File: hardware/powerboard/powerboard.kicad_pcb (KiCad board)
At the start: 4 copper layers, 81.2 x 50.7 mm, 72 parts, among them J1 USB_B_Micro, J10 5V, J11 3V3, J2 Boot, J3 Keysboard Header, J4 Display, J5 Debug, J7 UART_0, J8 I2C_0, J9 I2C_1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

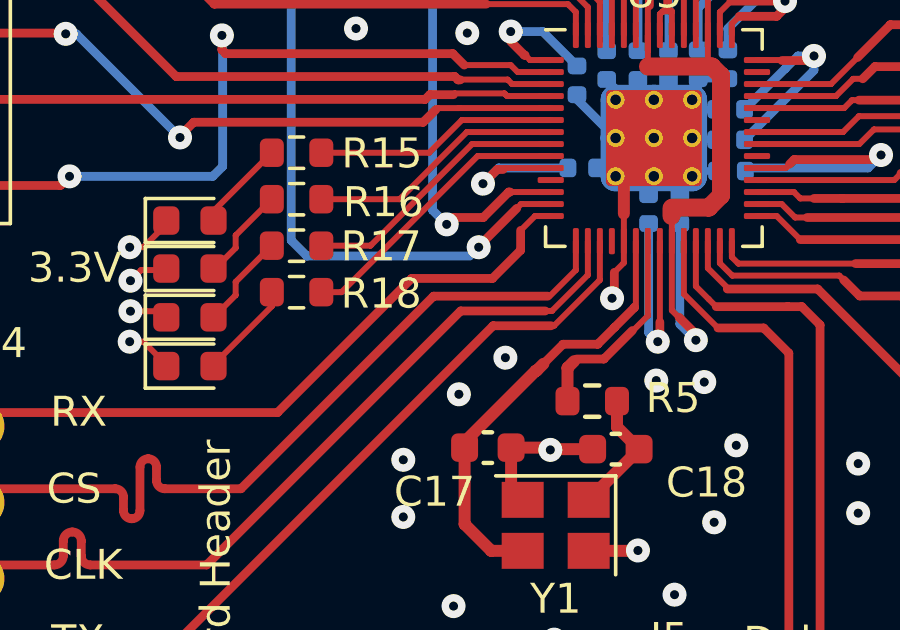
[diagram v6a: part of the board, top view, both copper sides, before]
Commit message: SPI_1 Pin error fixed
I'm a goof. The pins were off by 1. Rev. 1 will work with some additional wires. Rev. 2 will be ordered on my dime
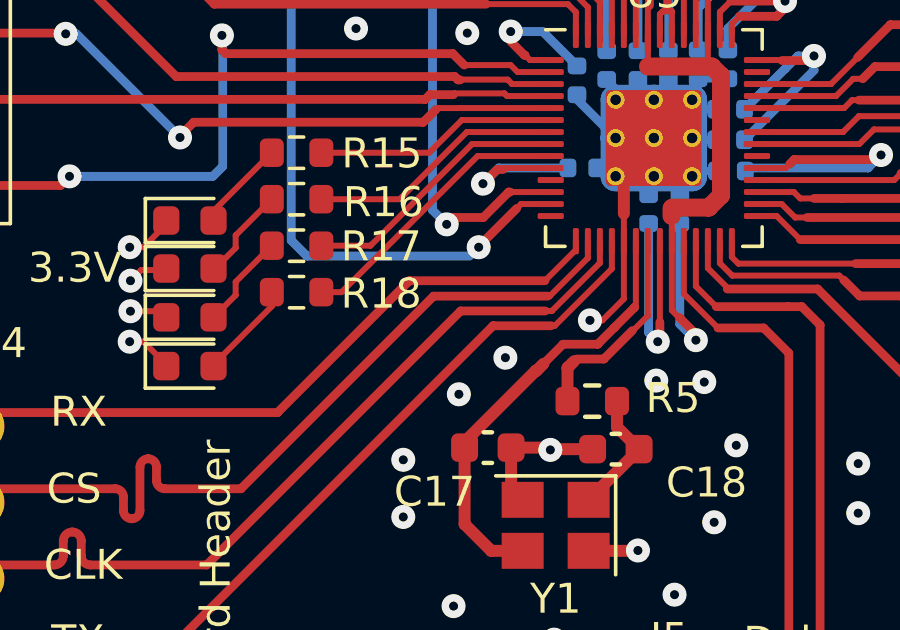
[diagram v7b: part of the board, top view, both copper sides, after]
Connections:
- U3 pad 14: SPI_RX_1 -> unconnected-(U3-Pad14)
- U3 pad 15: SPI_CS_1 -> SPI_RX_1
- U3 pad 16: SPI_SCLK_1 -> SPI_CS_1
- U3 pad 17: SPI_TX_1 -> SPI_SCLK_1
- U3 pad 18: unconnected-(U3-Pad18) -> SPI_TX_1
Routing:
- net GND: track 111.0 -> 112.3 mm

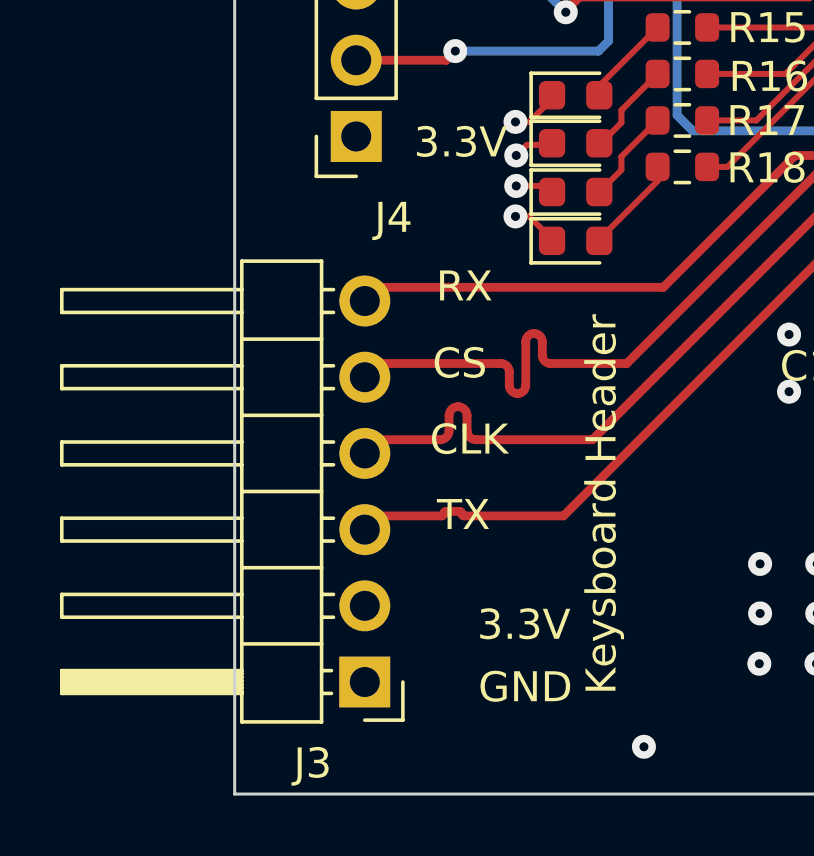
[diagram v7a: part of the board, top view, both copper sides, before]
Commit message: Rev.2 Boards Headers updated Male on Keysboard, Female on Brainboard
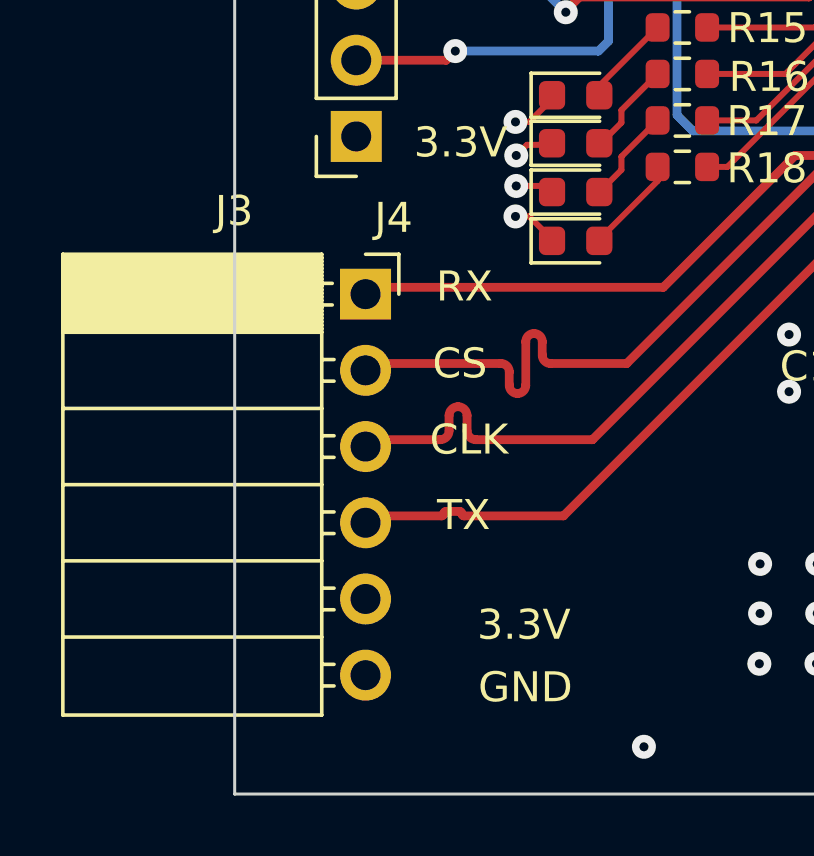
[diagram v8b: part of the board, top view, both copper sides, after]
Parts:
- J3: footprint Connector_PinHeader_2.54mm:PinHeader_1x06_P2.54mm_Horizontal -> Connector_PinSocket_2.54mm:PinSocket_1x06_P2.54mm_Horizontal
- moved J3 12.9 mm to (53.2, 49.2), turned to 0 degrees
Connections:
- J3 pad 1: GND -> SPI_RX_1
- J3 pad 2: +3.3V -> SPI_CS_1
- J3 pad 3: SPI_TX_1 -> SPI_SCLK_1
- J3 pad 4: SPI_SCLK_1 -> SPI_TX_1
- J3 pad 5: SPI_CS_1 -> +3.3V
- J3 pad 6: SPI_RX_1 -> GND
